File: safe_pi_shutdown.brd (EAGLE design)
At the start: 65 x 56 mm, 31 parts, among them U1 LTC2952CF

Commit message: prawie pierwsza wersja
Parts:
- added J1: 22-27-2021-02, con-molex:6410-02
- moved R15 42.7 mm to (47.5, 7.91)
- moved R14 41.5 mm to (51.1, 7.91), turned to 180 degrees
- moved C8 39.7 mm to (51.1, 6.45), turned to 180 degrees
- moved C7 38.0 mm to (58.8, 22.9), turned to 0 degrees
- moved C3 25.9 mm to (50.9, 23.9), turned to 180 degrees
- moved D6 24.8 mm to (50.1, 12.4), turned to 90 degrees
- moved U$1 21.1 mm to (47.2, 11.8)
- moved L1 18.1 mm to (42.8, 18.8), turned to 0 degrees
- moved C9 11.8 mm to (56.5, 12.4)
- moved S1 11.7 mm to (33.6, 18.4), turned to 90 degrees
- moved R4 11.6 mm to (56.6, 11.0)
- moved D2 11.5 mm to (36.4, 7.46), turned to 270 degrees
- moved T3 10.5 mm to (53.9, 18.7), flipped to the bottom, turned to 90 degrees
- moved R3 10.2 mm to (56.5, 9.59), turned to 180 degrees
- moved D1 9.60 mm to (36.4, 9.28), turned to 270 degrees
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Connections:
- removed net N$7: S1.3, U1.7
- new net N$5: J1.1, S1.3, S1.4, U1.7
- net GND: now also J1.2, X2.1; no longer X2.2
- net V1: now also X2.2; no longer X2.1
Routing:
- net GND: track 23.7 -> 116.8 mm, vias 0 -> 1
- net N$5: track 0.00 -> 27.2 mm
- net N$3: track 0.00 -> 19.2 mm, vias 0 -> 1
- net N$4: track 0.00 -> 17.2 mm
- net V2: track 26.7 -> 41.8 mm, vias 0 -> 2
- net N$13: track 0.00 -> 13.8 mm
- net N$17: track 18.4 -> 6.38 mm, vias 2 -> 1
- net VCC: track 32.6 -> 43.2 mm, vias 1 -> 2
- net N$18: track 27.4 -> 36.7 mm, vias 0 -> 2
- net N$6: track 1.93 -> 9.23 mm, vias 0 -> 1
- net N$2: track 5.65 -> 11.7 mm
- net N$21: track 0.00 -> 4.55 mm
- net N$10: track 17.3 -> 13.8 mm
- net N$19: track 19.2 -> 16.4 mm, vias 0 -> 1
- net N$8: track 6.17 -> 8.25 mm, vias 0 -> 1
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- removed copper zone on layer 1, net V2

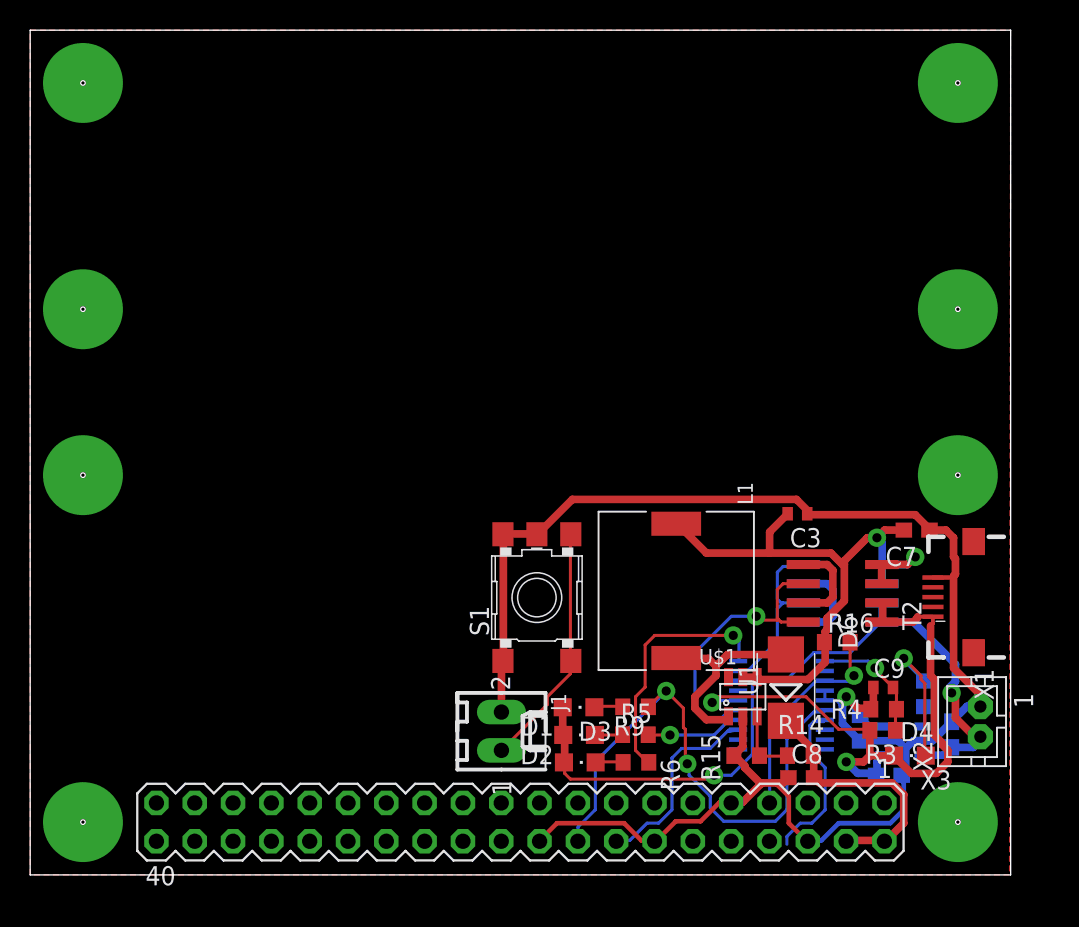
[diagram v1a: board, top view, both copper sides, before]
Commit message: polaczone wszystkie sciezki
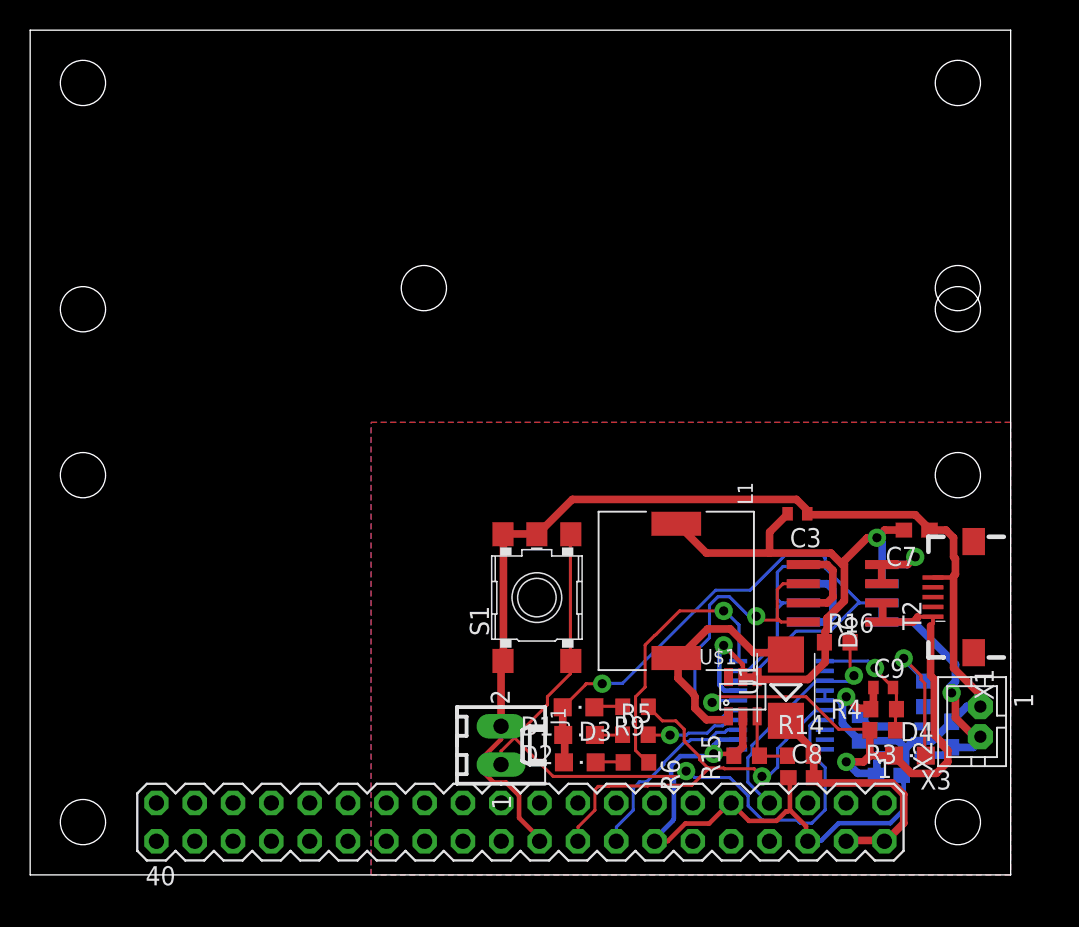
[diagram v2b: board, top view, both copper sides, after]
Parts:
- moved J1 0.94 mm to (31.2, 8.59)
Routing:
- net N$5: track 27.2 -> 48.4 mm, vias 0 -> 1
- net GND: track 116.8 -> 129.6 mm, vias 1 -> 2
- net N$18: track 36.7 -> 28.8 mm, vias 2 -> 1
- net V1: track 51.5 -> 59.0 mm
- net VCC: track 43.2 -> 50.0 mm, vias 2 -> 3
- net N$13: track 13.8 -> 16.3 mm
- net N$3: track 19.2 -> 21.6 mm
- net N$19: track 16.4 -> 18.4 mm
- net N$12: track 14.4 -> 15.6 mm
- net N$10: track 13.8 -> 12.7 mm
- added copper zone on layer 16, net GND

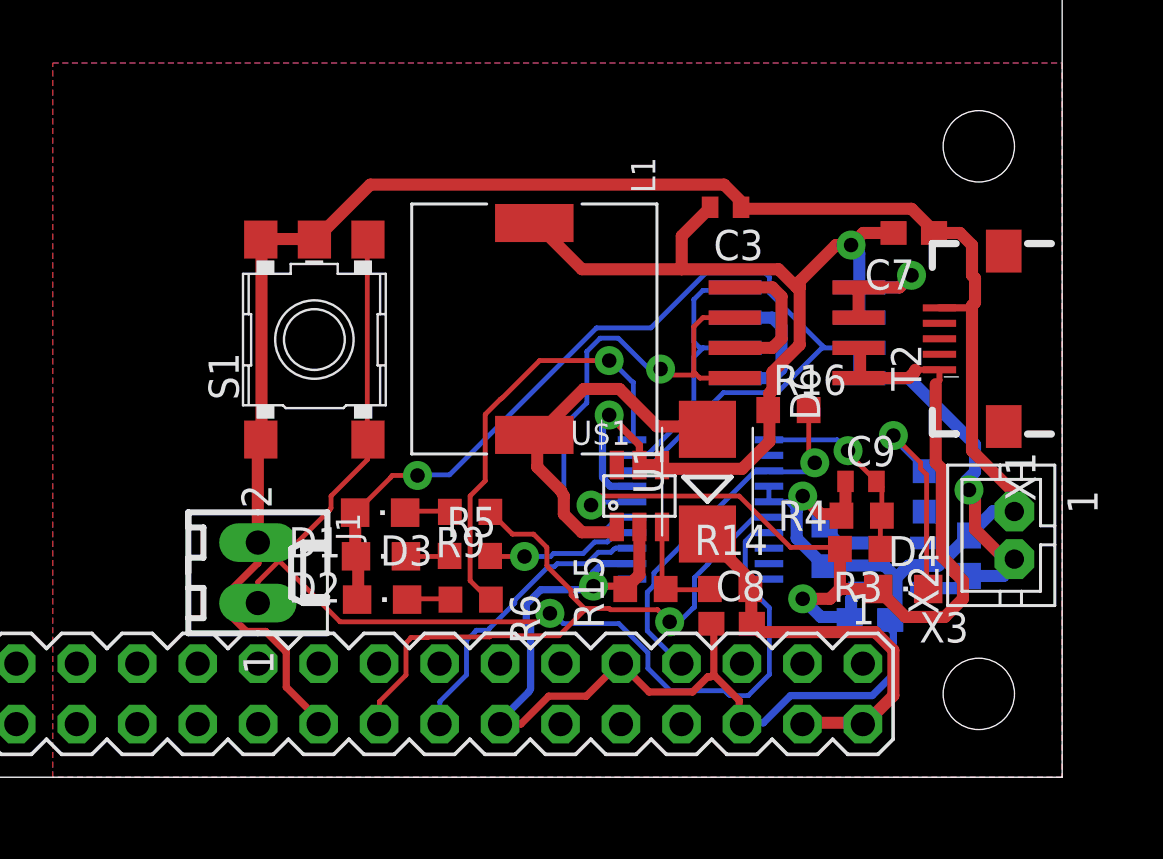
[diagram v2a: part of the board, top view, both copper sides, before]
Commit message: rozmieszczenie nazw na layaoucie
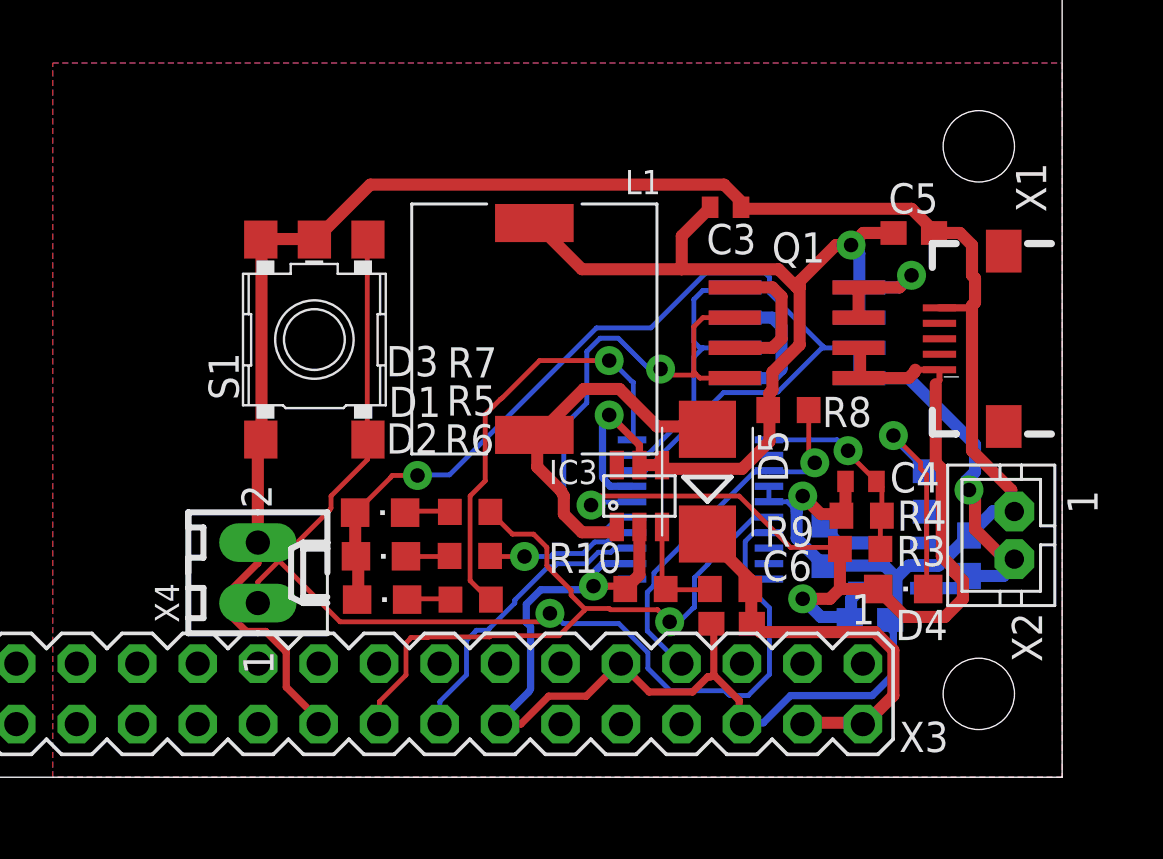
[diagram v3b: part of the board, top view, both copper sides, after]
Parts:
- removed C7: 10u, rcl:C0603
- removed C9: 100n, rcl:C0402
- removed R11: 10k, rcl:R0603
- removed R14: 910k, rcl:R0603
- added C1, C2: 10u, rcl:C0603
- added R1, R7: 1k, rcl:R0603
- C4: value 10u -> 100n; device rcl:C0603 -> rcl:C0402
- Q1, Q2: value (none) -> IRF7342
- R2: value 1k -> 10k
- R9: value 1k -> 910k
- moved C5 13.8 mm to (58.8, 22.9), flipped to the top, turned to 0 degrees
- moved R9 11.4 mm to (51.1, 7.91)
- moved C4 5.83 mm to (56.5, 12.4), flipped to the top, turned to 0 degrees
- moved R2 4.83 mm to (55.0, 9.72), turned to 270 degrees
- renumbered C8 to C6, D6 to D5, J1 to X4, R15 to R10, R16 to R8, T2 to Q1, T3 to Q2, U$1 to IC3, U$2 to IC1, U1 to IC2
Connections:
- net GND: now also C1.2, C2.2, C4.1, R2.2; no longer C4.2, C7.2, C9.1, R11.2
- net N$14: now also R2.1; no longer R11.1
- net N$15: now also R7.2; no longer R9.2
- net N$18: now also R7.1; no longer R9.1
- net N$21: now also R9.2; no longer R14.2
- net N$23: now also R1.1; no longer R2.1
- net N$4: now also R9.1; no longer R14.1
- net N$6: now also R1.2; no longer R2.2
- net N$8: now also C4.2; no longer C9.2
- net V1: now also C2.1; no longer C5.1
- net V2: now also C1.1; no longer C4.1
- net VCC: now also C5.1; no longer C7.1

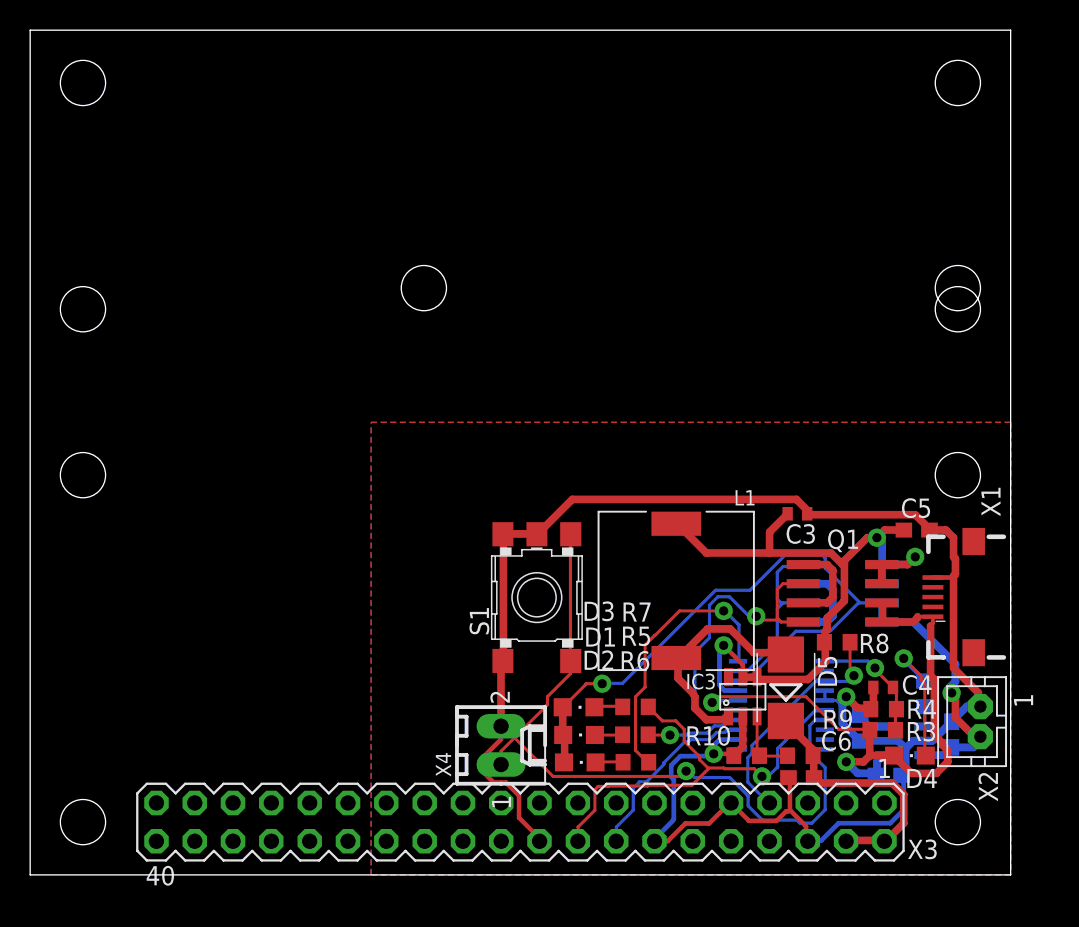
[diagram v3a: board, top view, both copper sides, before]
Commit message: dostosowanie do nanopi zero (pozycja konektora)
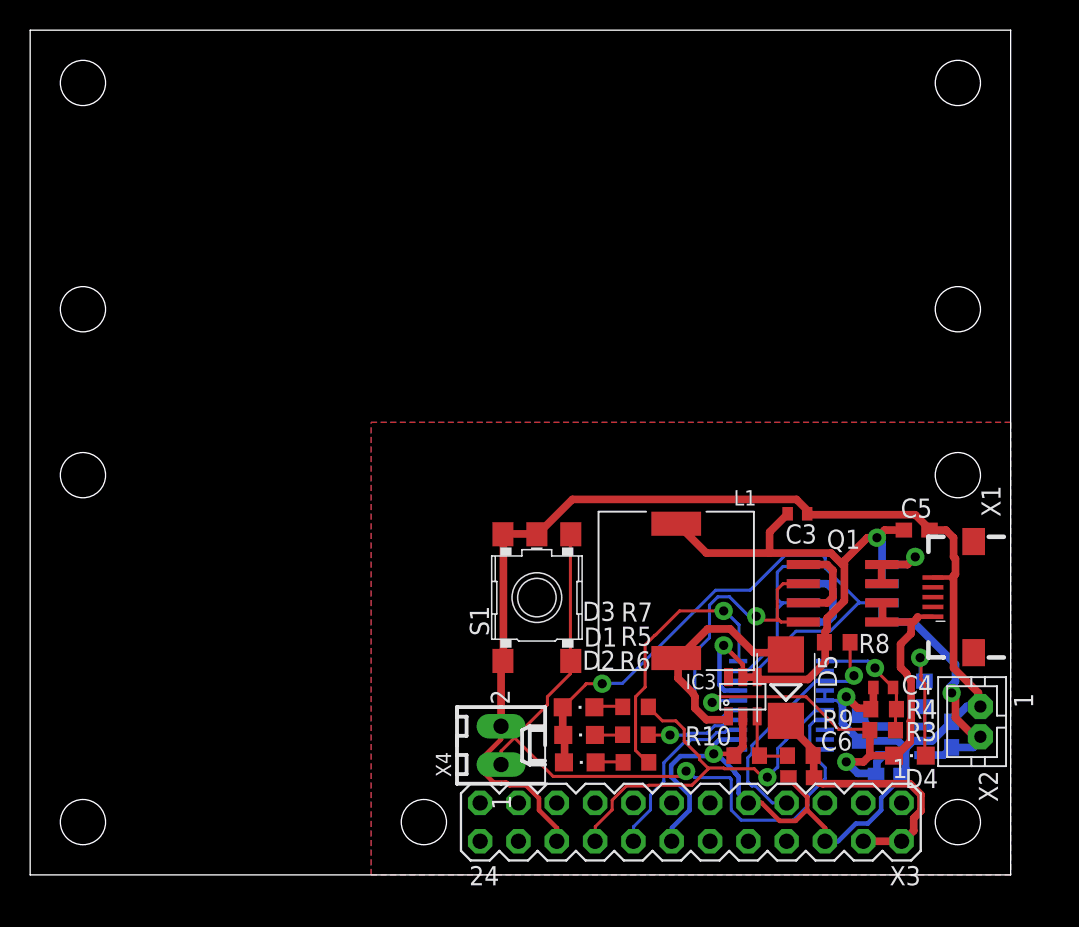
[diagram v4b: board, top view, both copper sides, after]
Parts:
- X3: device con-lstb:MA20-2 -> con-lstb:MA12-2
- moved X3 11.3 mm to (43.8, 3.50)
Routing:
- net V2: track 41.8 -> 37.2 mm
- net GND: track 129.6 -> 128.0 mm
- net N$18: track 28.8 -> 27.3 mm
- net N$12: track 15.6 -> 16.7 mm
- net N$4: track 17.2 -> 18.3 mm
- net N$10: track 12.7 -> 11.9 mm
- net N$6: track 9.23 -> 8.43 mm

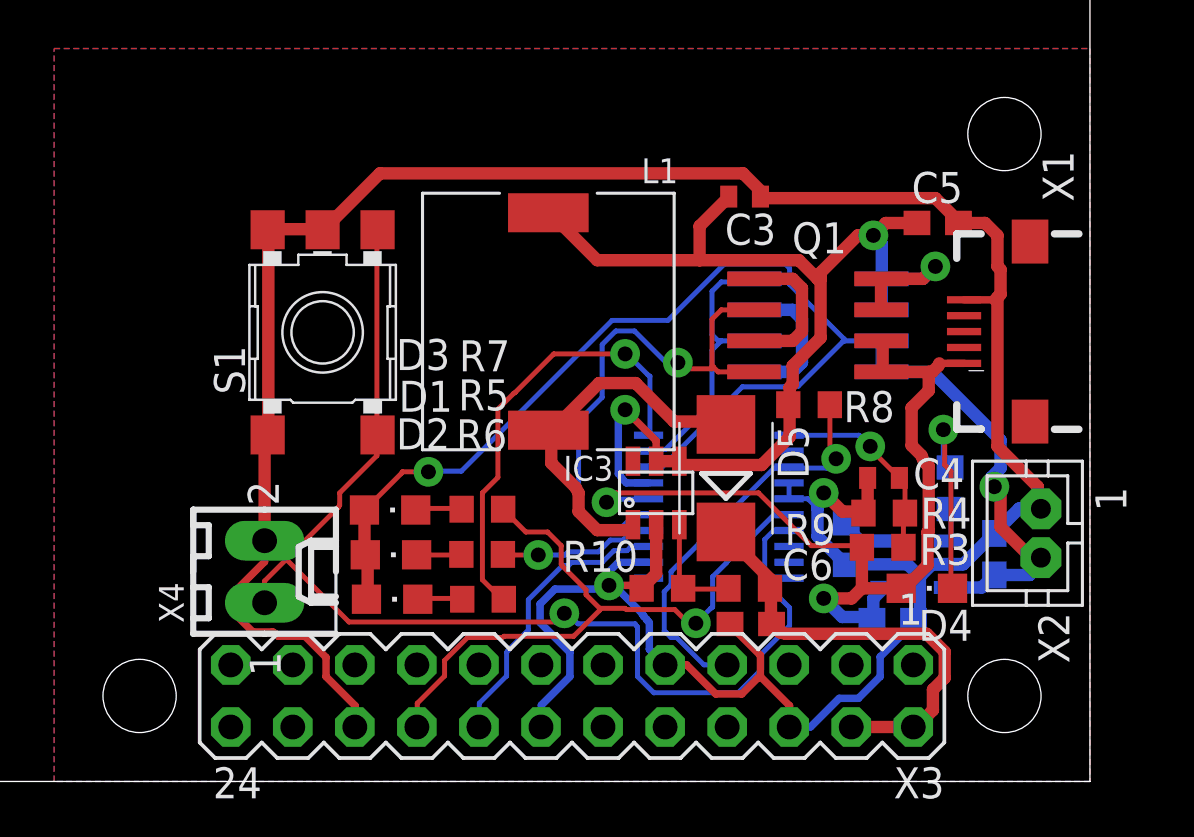
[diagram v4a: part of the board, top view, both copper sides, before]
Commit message: dodanie headerow do podlaczenia do plyty bazowej
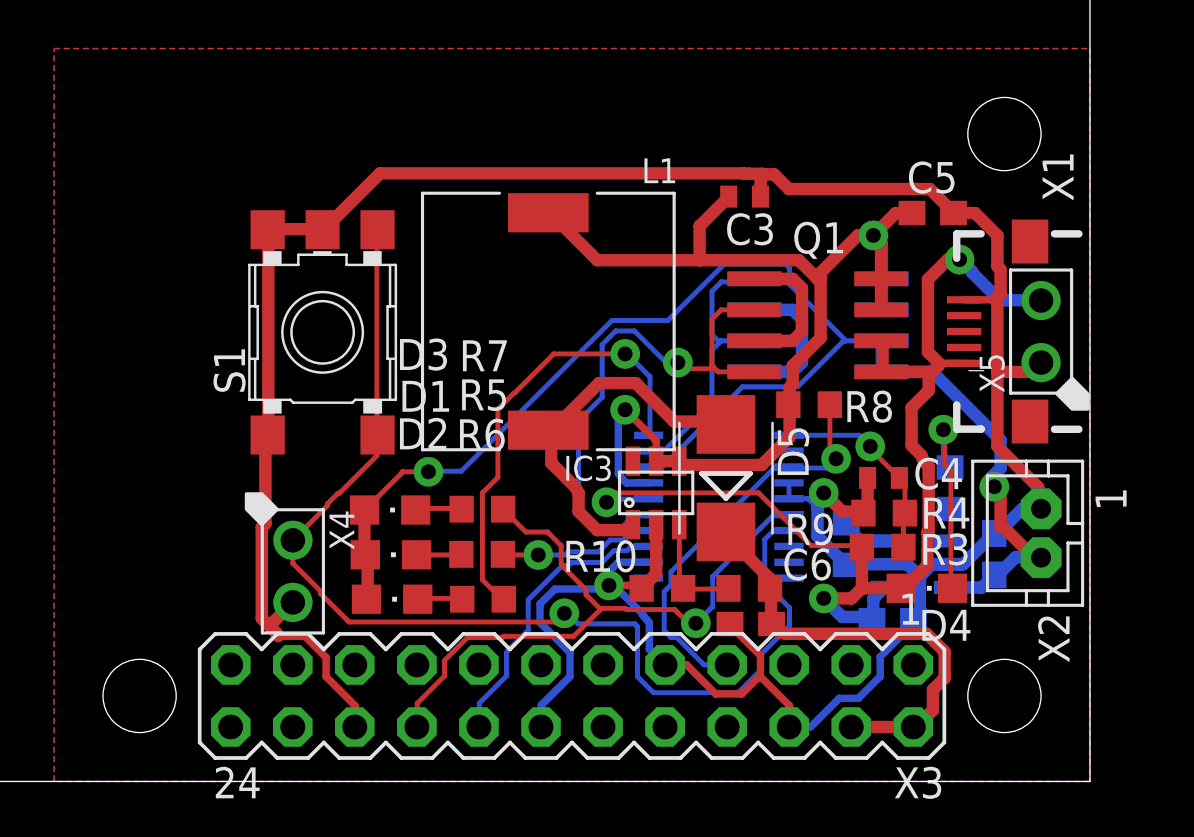
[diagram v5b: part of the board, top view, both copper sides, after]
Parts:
- added X5: MF-CON-2.54mm-01x02, MF_Connectors:PTH_2.54MM_01X02
- X4: value 22-27-2021-02 -> MF-CON-2.54mm-01x02; device con-molex:6410-02 -> MF_Connectors:PTH_2.54MM_01X02
- moved X4 1.16 mm to (32.4, 8.60)
- moved C5 0.45 mm to (58.6, 23.3)
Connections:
- net GND: now also X4.P$2, X5.P$1; no longer X4.2
- net N$5: now also X4.P$1; no longer X4.1
- net V2: now also X5.P$2
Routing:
- net V2: track 37.2 -> 46.5 mm, vias 2 -> 3
- net GND: track 128.0 -> 131.0 mm
- net VCC: track 50.0 -> 47.3 mm, vias 3 -> 2
- net N$5: track 48.2 -> 45.8 mm
